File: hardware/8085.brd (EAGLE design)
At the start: 167.9 x 122.5 mm, 34 parts, among them IC2 74AC573N, IC3 ATF16V8BP3, IC4 74HCT245N, IC5 74HCT245DW, IC9 74HCT138N

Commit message: PCB updated
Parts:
- removed IC4: 74HCT245N, 74xx-eu:DIL20
- added Q1: (no value), crystal:HC49/S
- moved C18 83.2 mm to (33.3, 98.4)
- moved C11 24.0 mm to (29.5, 36.2), turned to 0 degrees
- moved IC3 14.6 mm to (95.2, 15.9)
- moved C14 14.6 mm to (101.6, 28.7)
- moved IC1 11.4 mm to (40.6, 60.3)
- moved IC5 11.4 mm to (41.3, 92.7)
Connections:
- new net N$1: IC1.1, Q1.2
- new net N$2: IC1.2, Q1.1
- net D0: no longer IC4.2
- net D1: no longer IC4.3
- net D2: no longer IC4.4
- net D3: no longer IC4.5
- net D4: no longer IC4.6
- net D5: no longer IC4.7
- net D6: no longer IC4.8
- net D7: no longer IC4.9
- net GND: no longer IC4.10
- net VCC: no longer IC4.20
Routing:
- net A15: track 224.1 -> 196.1 mm
- net LOCAL_IO_CS: track 76.9 -> 52.9 mm
- net !IORQ: track 70.6 -> 51.8 mm, vias 1 -> 0
- net VCC: track 303.4 -> 287.5 mm
- net ROM_SHADOWING: track 115.6 -> 101.0 mm
- net CS_EPROM: track 83.9 -> 69.9 mm
- net D5: track 165.5 -> 153.0 mm
- net D3: track 151.1 -> 138.7 mm
- net D7: track 172.8 -> 160.3 mm
- net D6: track 165.6 -> 153.1 mm
- net D2: track 157.1 -> 144.6 mm
- net D1: track 183.3 -> 170.8 mm
- net D0: track 163.0 -> 150.6 mm
- net D4: track 161.4 -> 148.9 mm
- net INTA: track 96.5 -> 84.1 mm
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
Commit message: PCB updated
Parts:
- removed LED1, LED2: (no value), led:LED3MM
- removed R1: 1k, rcl:M1206
- removed R7, R8: 470R, rcl:R0603
- removed U$1: UCY74S412, mw:DIL24-6
- added IC10: 74HCT00N, 74xx-eu:DIL14
- added IC4: 74AC00D, 74xx-eu:SO14
- added IC6: 74AC273N, 74xx-eu:DIL20
- added IC7: 74HCT139N, 74xx-eu:DIL16
- added IC8: 7404N, 74xx-us:DIL14
- added LED3, LED4: (no value), led:LED5MM
- added R2, R3: (no value), rcl:R1206
- C1, C14, C2, C3, C6: device rcl:C1206 -> rcl:C0805
- R9: device rcl:0204/7 -> rcl:M1206
- moved C12 106.9 mm to (124.5, 28.3), turned to 90 degrees
- moved C22 103.4 mm to (34.4, 109.9), turned to 0 degrees
- moved C6 79.3 mm to (87.8, 28.2), turned to 90 degrees
- moved C9 15.5 mm to (105.6, 102.9), turned to 0 degrees
- moved IC3 14.0 mm to (81.3, 15.9)
- moved R9 11.9 mm to (144.5, 23.8), flipped to the bottom
- moved C10 5.43 mm to (129.5, 111.8), turned to 270 degrees
- moved C11 4.72 mm to (33.0, 33.0), turned to 270 degrees
- moved C15 4.42 mm to (150.8, 115.9), turned to 90 degrees
- moved C14 2.27 mm to (103.8, 28.3)
- moved IC9 1.91 mm to (144.5, 16.5)
- moved C13 1.27 mm to (148.3, 28.3)
- moved C1 0.95 mm to (78.1, 48.5)
- moved C2 0.95 mm to (98.4, 48.5)
- moved C3 0.95 mm to (118.7, 48.4)
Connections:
- net HALT renamed HRQ
- removed net !CS_PORT_OUT: U$1.13
- removed net !IORQ: IC3.4, IC9.4
- removed net !MREQ: IC3.1
- removed net A14_IN: IC1.27, IC5.17
- removed net A15_IN: IC1.28, IC5.18
- removed net BUSAK: SV2.38
- removed net BUSRQ: SV2.37
- removed net CS_RAM1: IC3.19, U$4.20
- removed net DMA_CS: IC3.14
- removed net DMA_RDY: SV2.40
- removed net M1: IC3.5
- removed net N$17: LED2.K, R8.2
- removed net N$3: R7.1, U$1.19
- removed net N$4: LED1.K, R7.2
- removed net N$6: R8.1, U$1.21
- removed net N$7: R1.2, U$1.2
- removed net NMI: SV2.39
- removed net PORT_CS: IC3.15
- removed net ROM_SHADOWING: IC3.2, U$1.8
- removed net WAIT: SV2.42
- new net !A15: IC7.1, IC8.2
- new net A14_CPU: IC1.27, IC4.10, IC4.9
- new net A14_SWITCH: IC4.6, IC5.17
- new net A15_CPU: IC1.28, IC4.12, IC4.13
- new net A15_SWITCH: IC4.3, IC5.18
- new net AEN: IC2.1, IC5.19, IC9.4, SV2.42
- new net BANK_A14: IC10.6, U$2.1
- new net IO_M: IC1.34, IC3.4
- new net IO_RD: IC3.19, SV2.34
- new net IO_WR: IC3.18, SV2.35
- new net MEM_RD: IC3.17, SV2.39, U$2.22, U$3.22, U$4.22
- new net MEM_WR: IC3.16, SV2.40, U$2.27, U$4.27
- new net N$10: IC6.19, R2.1
- new net N$19: IC7.15, IC7.4
- new net N$21: IC4.5, IC4.8
- new net N$26: IC4.1, IC4.11
- new net N$5: IC6.16, R3.1
- new net N$8: LED3.K, R2.2
- new net N$9: LED4.K, R3.2
- new net RESET: IC1.3, IC8.3, SV2.37
- new net START_MEM_SWITCH: IC4.2, IC4.4, IC6.6
- net !RESET: now also IC6.1, IC8.4; no longer U$1.14
- net 8275_DACK: now also IC10.5
- net A13: now also IC7.14
- net A14: now also IC7.2; no longer U$2.1
- net A15: now also IC8.1, U$4.20; no longer IC3.3
- net A4: no longer IC3.7
- net CS_EPROM: now also IC7.5; no longer IC3.17
- net CS_RAM2: now also IC7.12; no longer IC3.18
- net D0: now also IC6.3; no longer U$1.3
- net D1: now also IC6.4; no longer U$1.5
- net D2: now also IC6.7; no longer U$1.7
- net D3: now also IC6.8; no longer U$1.9
- net D4: now also IC6.13; no longer U$1.16
- net D5: now also IC6.14; no longer U$1.18
- net D6: now also IC6.17; no longer U$1.20
- net D7: now also IC6.18; no longer U$1.22
- net GND: now also IC10.1, IC10.10, IC10.12, IC10.13, IC10.2, IC10.7, IC10.9, IC4.7, IC6.10, IC7.13, IC7.3, IC7.8, IC8.11, IC8.13, IC8.5, IC8.7, IC8.9; no longer IC2.1, IC5.19, U$1.12
- net HLDA: now also SV2.38
- net INT: now also IC1.10
- net INTA: now also IC1.11; no longer IC3.16
- net LOCAL_IO_CS: no longer IC3.6
- net OUT_1: now also IC6.12; no longer U$1.15
- net OUT_2: now also IC6.15; no longer U$1.17
- net OUT_3: now also IC6.9; no longer U$1.10
- net OUT_4: now also IC6.5; no longer U$1.6
- net RD: now also IC3.3; no longer SV2.34, U$2.22, U$3.22, U$4.22
- net SET_BANK_A14: now also IC10.4, IC6.2; no longer U$1.4
- net VCC: now also IC10.14, IC4.14, IC6.20, IC7.16, IC8.14, LED3.A, LED4.A; no longer LED1.A, LED2.A, R1.1, U$1.24
- net WR: now also IC3.2; no longer SV2.35, U$1.1, U$2.27, U$4.27
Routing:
- net AEN: track 0.00 -> 215.7 mm, vias 0 -> 6
- net WR: track 187.6 -> 0.00 mm, vias 4 -> 0
- net RD: track 173.2 -> 0.00 mm, vias 4 -> 0
- net MEM_RD: track 0.00 -> 172.5 mm, vias 0 -> 4
- net MEM_WR: track 0.00 -> 141.2 mm, vias 0 -> 4
- net RESET: track 0.00 -> 134.6 mm, vias 0 -> 2
- net HLDA: track 0.00 -> 134.3 mm
- net VCC: track 287.5 -> 412.6 mm, vias 4 -> 3
- net ROM_SHADOWING: track 101.0 -> 0.00 mm, vias 2 -> 0
- net WAIT: track 98.0 -> 0.00 mm, vias 1 -> 0
- net IO_RD: track 0.00 -> 95.1 mm, vias 0 -> 2
- net NMI: track 94.4 -> 0.00 mm, vias 1 -> 0
- net IO_WR: track 0.00 -> 93.3 mm, vias 0 -> 2
- net START_MEM_SWITCH: track 0.00 -> 88.5 mm, vias 0 -> 2
- net BUSAK: track 81.3 -> 0.00 mm
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
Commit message: PCB updated
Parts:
- added IC11: 74HCT245DW, 74xx-eu:SO20W
- added IC12: DS1813, ds1813_revised:TO-92
- added JP1: (no value), pinhead:1X02
- added R1, R4, R5, R6: (no value), rcl:R0603
- added SV1: (no value), con-ml:ML40
- C21: device rcl:C1206 -> rcl:C0603
- moved C21 63.4 mm to (51.4, 59.1)
- moved C5 46.3 mm to (-9.53, -19.1)
- moved C23 45.1 mm to (-13.7, -28.6)
- moved C16 40.3 mm to (-13.7, -12.6)
- moved C11 3.81 mm to (29.2, 33.0)
- moved IC1 3.81 mm to (36.8, 60.3)
- moved IC2 3.81 mm to (55.2, 73.0)
- moved IC4 3.81 mm to (36.8, 106.0)
- moved IC5 3.81 mm to (37.5, 92.7)
- moved Q1 3.81 mm to (48.9, 37.5)
- moved C22 3.49 mm to (30.9, 109.9)
- moved C18 2.25 mm to (31.8, 100.0)
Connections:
- removed net HOLD: IC1.39
- new net CF_BDV2_LED: SV1.39
- new net CF_BVD1: SV1.34
- new net CF_CE1: SV1.37
- new net CF_CE2: SV1.38
- new net CF_INPACK: SV1.21
- new net CF_RDY_CSY_IREQ: SV1.31
- new net CF_REG: SV1.29
- new net CF_WAIT: SV1.27
- new net CF_WP_IOCS16: SV1.32
- new net D0_CF: IC11.18, SV1.17
- new net D1_CF: IC11.17, SV1.15
- new net D2_CF: IC11.16, SV1.13
- new net D3_CF: IC11.15, SV1.11
- new net D4_CF: IC11.14, SV1.9
- new net D5_CF: IC11.13, SV1.7
- new net D6_CF: IC11.12, SV1.5
- new net D7_CF: IC11.11, SV1.3
- new net LOCAL_PORT_CS: IC3.15, IC6.11
- new net N$3: IC1.9, R1.1
- new net N$4: IC1.8, R4.1
- new net N$6: IC1.7, R5.1
- new net N$7: IC1.6, R6.1
- new net RES_IN: IC1.36, IC12.1, JP1.2
- net !RESET: now also SV1.1
- net A0: now also SV1.35
- net A1: now also SV1.33
- net A2: now also SV1.36
- net A4: now also IC3.2
- net D0: now also IC11.2
- net D1: now also IC11.3
- net D2: now also IC11.4
- net D3: now also IC11.5
- net D4: now also IC11.6
- net D5: now also IC11.7
- net D6: now also IC11.8
- net D7: now also IC11.9
- net GND: now also IC11.10, IC12.3, JP1.1, R1.2, R4.2, R5.2, R6.2, SV1.19, SV1.2, SV1.22, SV1.24, SV1.26
- net HRQ: now also IC1.39
- net IO_M: now also IC3.3; no longer IC3.4
- net IO_RD: now also SV1.25
- net IO_WR: now also SV1.23
- net LOCAL_IO_CS: now also IC3.6
- net RD: now also IC3.4; no longer IC3.3
- net RDYIN: now also IC1.35
- net VCC: now also IC11.20, IC12.2
- net WR: now also IC3.5; no longer IC3.2
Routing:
- net RDYIN: track 0.00 -> 201.7 mm, vias 0 -> 4
- net LOCAL_PORT_CS: track 0.00 -> 141.6 mm, vias 0 -> 2
- net WR: track 0.00 -> 111.1 mm
- net RD: track 0.00 -> 106.0 mm
- net VCC: track 412.6 -> 511.5 mm, vias 3 -> 6
- net IO_M: track 0.00 -> 98.3 mm
- net !RESET: track 135.4 -> 212.7 mm, vias 4 -> 6
- net IO_RD: track 95.1 -> 170.4 mm, vias 2 -> 4
- net IO_WR: track 93.3 -> 163.5 mm, vias 2 -> 4
- net LOCAL_IO_CS: track 0.00 -> 65.0 mm
- net A4: track 114.8 -> 165.6 mm, vias 2 -> 4
- net HRQ: track 92.5 -> 134.5 mm
- net AEN: track 215.7 -> 226.5 mm
- net RES_IN: track 0.00 -> 9.53 mm
- net N$26: track 16.1 -> 24.5 mm
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
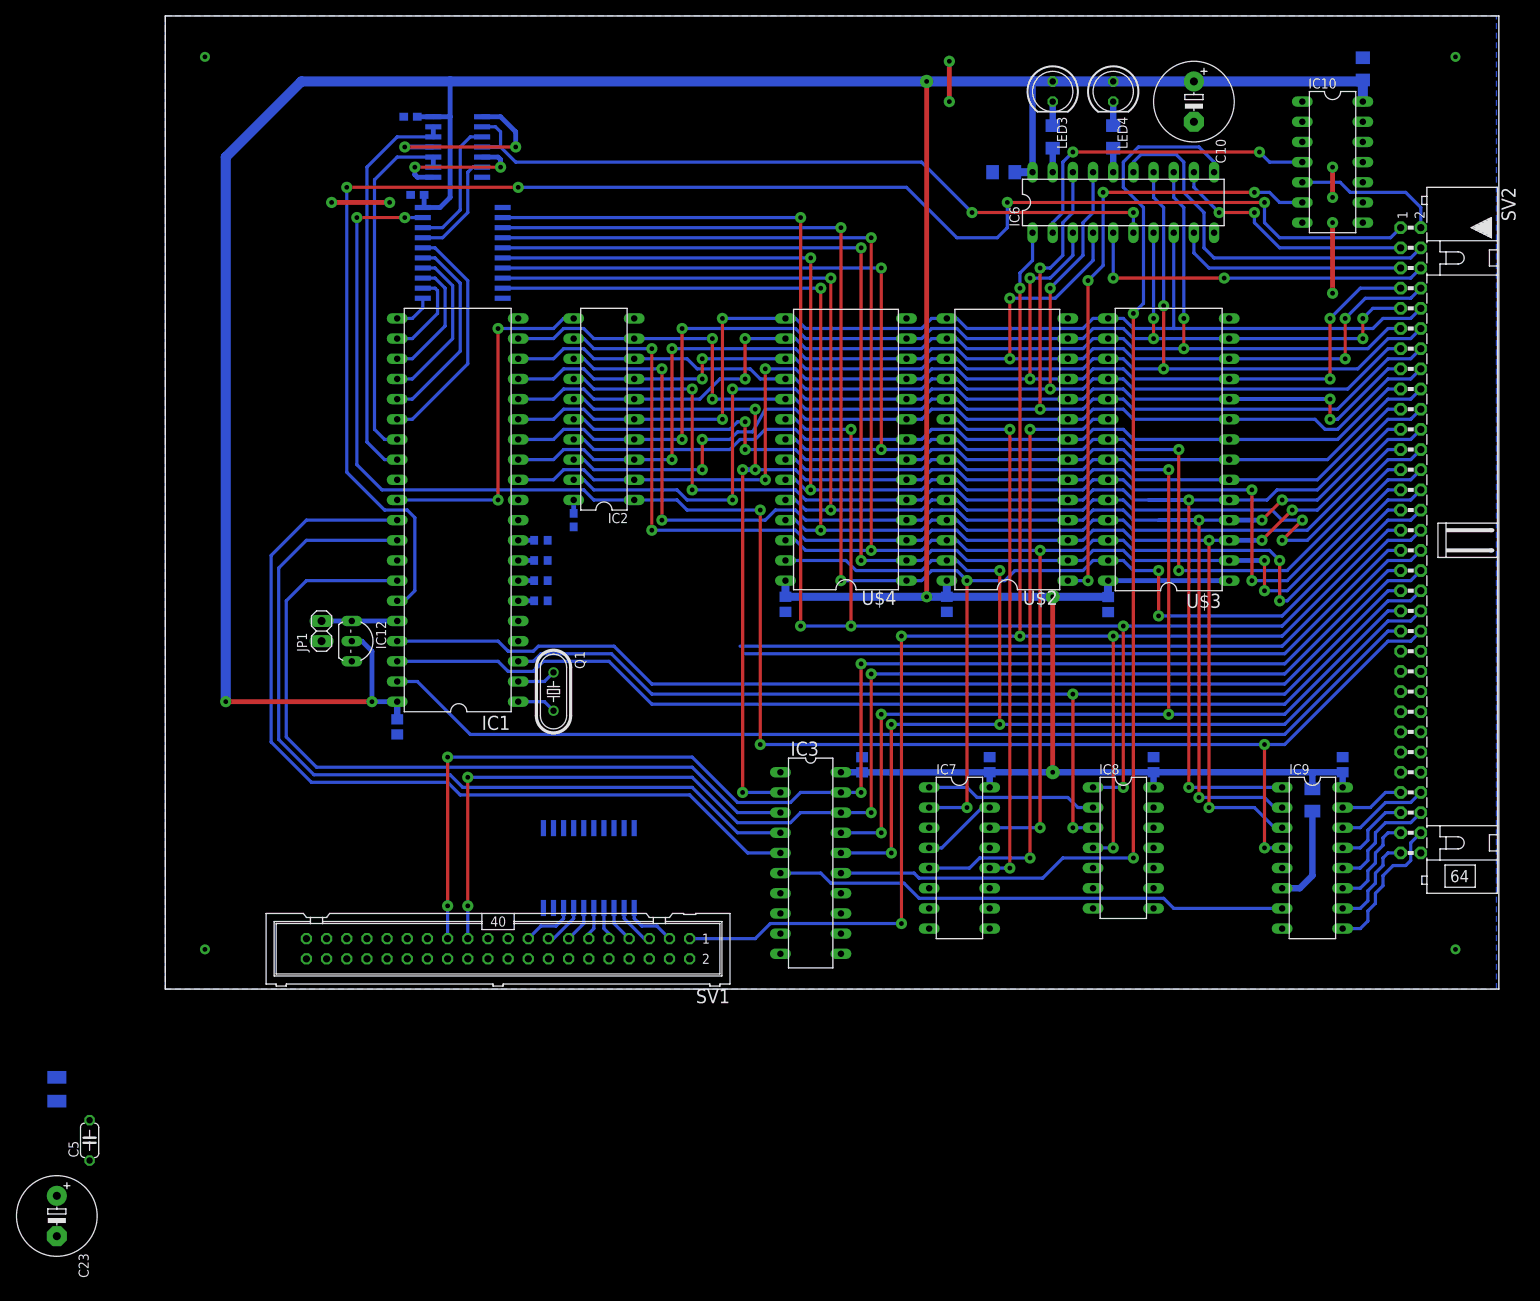
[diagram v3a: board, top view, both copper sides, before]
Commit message: Reset circuit simplified
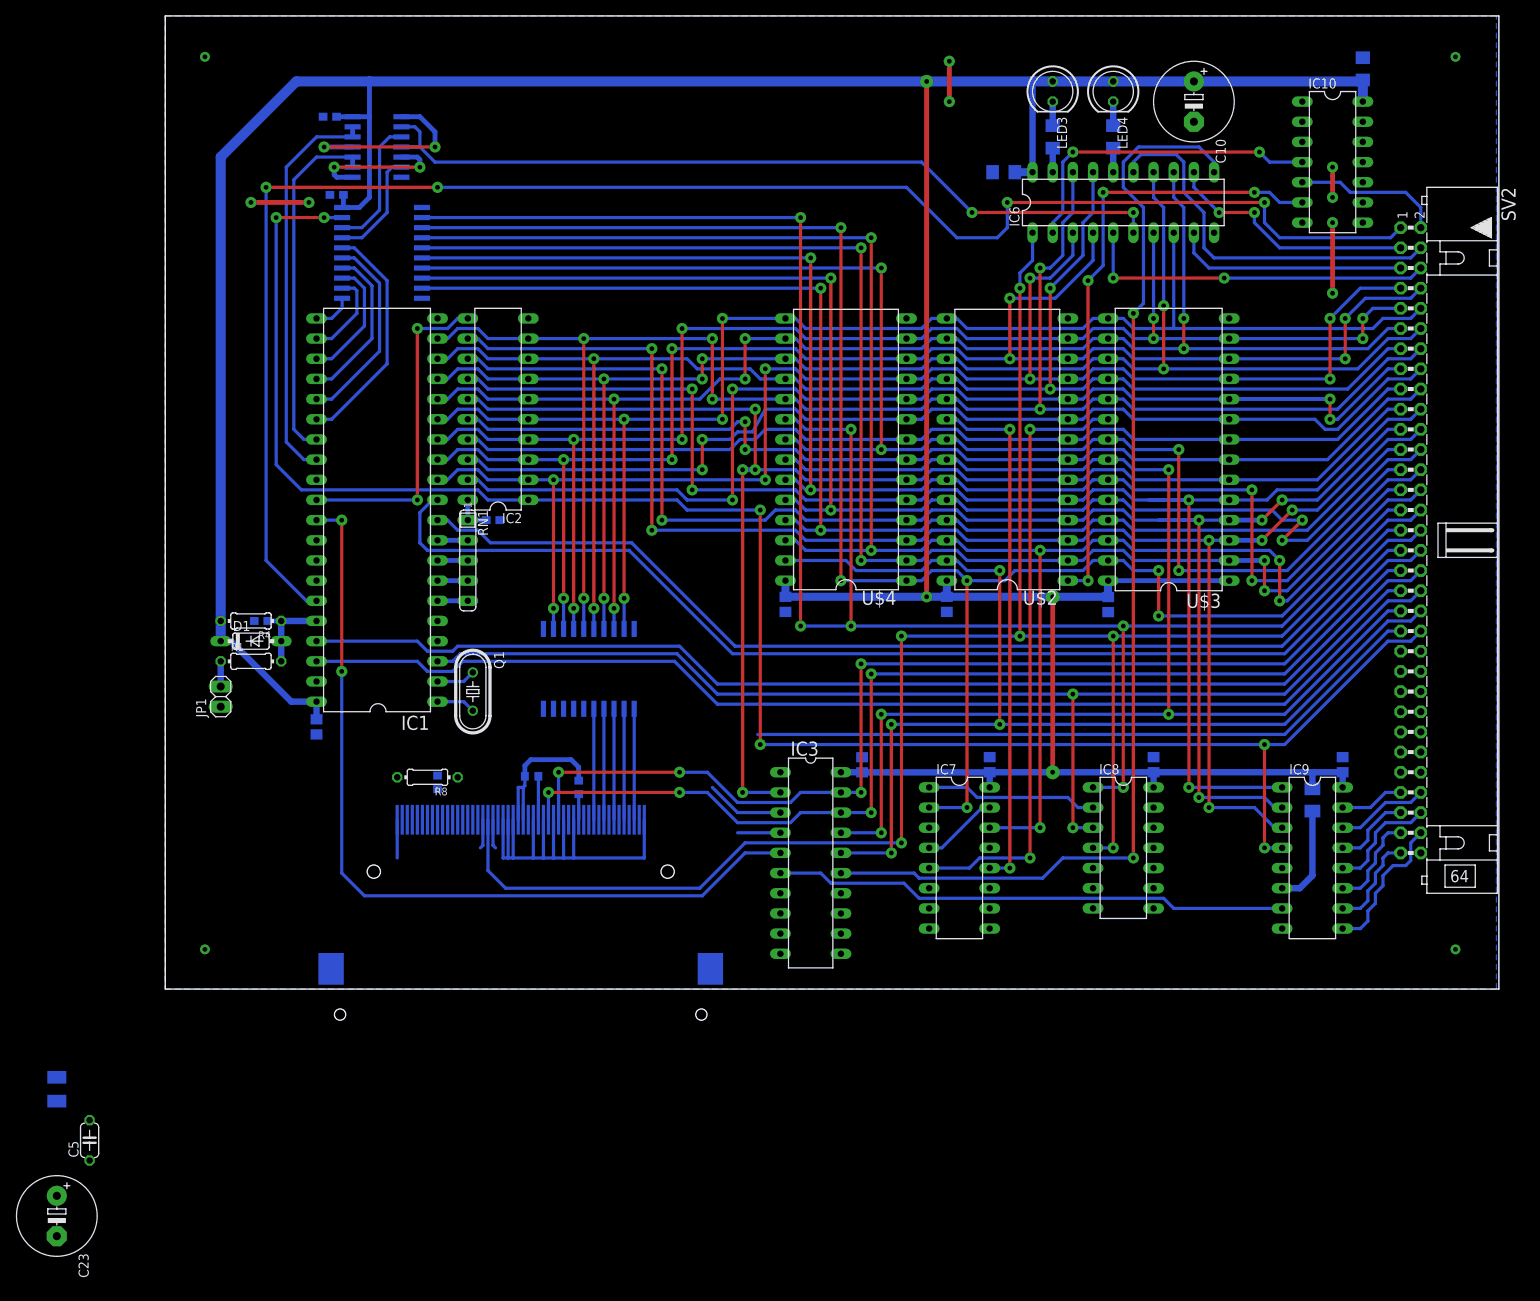
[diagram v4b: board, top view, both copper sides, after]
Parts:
- removed IC12: DS1813, ds1813_revised:TO-92
- removed R5, R6: (no value), rcl:R0603
- removed SV1: (no value), con-ml:ML40
- added C4: (no value), rcl:C0603
- added CON1: (no value), con-hirose:MI20-50PD-SF
- added D1: 1N4148DO35-7, diode:DO35-7
- added R10, R11, R7: (no value), rcl:R0603
- added R8: (no value), rcl:0204/7
- added RN1: (no value), resistor-sil:SIL5
- R1, R4: device rcl:R0603 -> rcl:0204/7
- moved R1 39.6 mm to (10.8, 41.3), flipped to the top, turned to 0 degrees
- moved R4 37.3 mm to (10.8, 46.4), flipped to the top
- moved IC11 25.1 mm to (53.3, 40.3)
- moved JP1 15.1 mm to (6.99, 36.8)
- moved IC2 13.3 mm to (41.9, 73.0)
- moved C21 10.2 mm to (41.3, 59.1), turned to 180 degrees
- moved IC5 10.2 mm to (27.3, 92.7)
- moved Q1 10.2 mm to (38.7, 37.5)
- moved C11 10.2 mm to (19.1, 33.0)
- moved C18 10.2 mm to (21.6, 100.0)
- moved C22 10.2 mm to (20.7, 109.9)
- moved IC1 10.2 mm to (26.7, 60.3)
- moved IC4 10.2 mm to (26.7, 106.0)
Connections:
- removed net CF_BDV2_LED: SV1.39
- removed net CF_BVD1: SV1.34
- removed net CF_CE1: SV1.37
- removed net CF_CE2: SV1.38
- removed net CF_INPACK: SV1.21
- removed net CF_RDY_CSY_IREQ: SV1.31
- removed net CF_REG: SV1.29
- removed net CF_WAIT: SV1.27
- removed net CF_WP_IOCS16: SV1.32
- removed net D0_CF: IC11.18, SV1.17
- removed net D1_CF: IC11.17, SV1.15
- removed net D2_CF: IC11.16, SV1.13
- removed net D3_CF: IC11.15, SV1.11
- removed net D4_CF: IC11.14, SV1.9
- removed net D5_CF: IC11.13, SV1.7
- removed net D6_CF: IC11.12, SV1.5
- removed net D7_CF: IC11.11, SV1.3
- new net CF_CS0: CON1.7
- new net CF_D0: CON1.21, IC11.18
- new net CF_D1: CON1.22, IC11.17
- new net CF_D2: CON1.23, IC11.16
- new net CF_D3: CON1.2, IC11.11
- new net CF_D4: CON1.3, IC11.12
- new net CF_D5: CON1.4, IC11.13
- new net CF_D6: CON1.5, IC11.14
- new net CF_D7: CON1.6, IC11.15
- new net N$11: CON1.44, R8.1
- new net N$12: CON1.36, R7.1
- new net N$13: CON1.46, R10.1
- new net N$14: JP1.2, R1.1
- new net N$29: CON1.32, R11.1
- net !RESET: now also CON1.41; no longer SV1.1
- net A0: now also CON1.20; no longer SV1.35
- net A1: now also CON1.19; no longer SV1.33
- net A2: now also CON1.18; no longer SV1.36
- net D3: now also IC11.9; no longer IC11.5
- net D4: now also IC11.8; no longer IC11.6
- net D6: now also IC11.6; no longer IC11.8
- net D7: now also IC11.5; no longer IC11.9
- net GND: now also C4.2, CON1.1, CON1.10, CON1.11, CON1.12, CON1.14, CON1.15, CON1.16, CON1.17, CON1.39, CON1.50, CON1.8, CON1.9; no longer IC12.3, R1.2, R4.2, R5.2, R6.2, SV1.19, SV1.2, SV1.22, SV1.24, SV1.26
- net IO_RD: now also CON1.34; no longer SV1.25
- net IO_WR: now also CON1.35; no longer SV1.23
- net N$3: now also RN1.2; no longer R1.1
- net N$4: now also RN1.3; no longer R4.1
- net N$6: now also RN1.4; no longer R5.1
- net N$7: now also RN1.5; no longer R6.1
- net RES_IN: now also C4.1, D1.A, R1.2, R4.1; no longer IC12.1, JP1.2
- net VCC: now also CON1.13, CON1.38, D1.C, R10.2, R11.2, R4.2, R7.2, R8.2, RN1.1; no longer IC12.2
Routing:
- net RD: track 106.0 -> 5.40 mm
- net IO_M: track 98.3 -> 9.89 mm
- net GND: track 25.1 -> 98.3 mm
- net INTA: track 87.9 -> 141.4 mm
- net HRQ: track 134.5 -> 86.4 mm
- net D7: track 160.4 -> 207.1 mm, vias 4 -> 6
- net INT: track 91.8 -> 136.5 mm
- net D6: track 147.5 -> 191.7 mm, vias 2 -> 4
- net D5: track 147.3 -> 188.9 mm, vias 4 -> 6
- net D4: track 144.7 -> 183.8 mm, vias 4 -> 6
- net D3: track 143.2 -> 179.7 mm, vias 2 -> 4
- net D2: track 145.2 -> 179.2 mm, vias 6 -> 8
- net IO_RD: track 170.4 -> 138.8 mm
- net D1: track 161.5 -> 193.0 mm, vias 6 -> 8
- net D0: track 160.1 -> 189.1 mm, vias 6 -> 8
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
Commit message: Minor optimizations
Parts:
- moved C23 154.6 mm to (51.1, 111.8)
- moved IC11 1.91 mm to (53.3, 42.2)
- moved C21 0.48 mm to (41.5, 59.5), turned to 270 degrees
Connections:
- net GND: now also RN1.1
- net VCC: no longer RN1.1
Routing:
- net HRQ: track 86.4 -> 161.3 mm, vias 0 -> 2
- net VCC: track 512.7 -> 568.0 mm, vias 4 -> 6
- net GND: track 98.3 -> 118.0 mm, vias 8 -> 10
- net D3: track 179.7 -> 177.8 mm
- net D6: track 191.7 -> 189.8 mm
- net D5: track 188.9 -> 187.0 mm
- net D2: track 179.2 -> 177.3 mm
- net D1: track 193.0 -> 191.1 mm
- net CF_D7: track 14.0 -> 15.9 mm
- net CF_D6: track 14.0 -> 15.9 mm
- net CF_D5: track 14.0 -> 15.9 mm
- net CF_D4: track 14.0 -> 15.9 mm
- net CF_D3: track 14.0 -> 15.9 mm
- net D7: track 207.1 -> 205.2 mm
- net D4: track 183.8 -> 181.9 mm
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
